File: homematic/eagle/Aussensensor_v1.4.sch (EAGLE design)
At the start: 41 parts, among them IC1 Atmega 328P, IC2 MAX1724, IC3 TSL2561, IC4 BMP180, IC5 BME280, IC6 DS18B20, T1 IRML6344

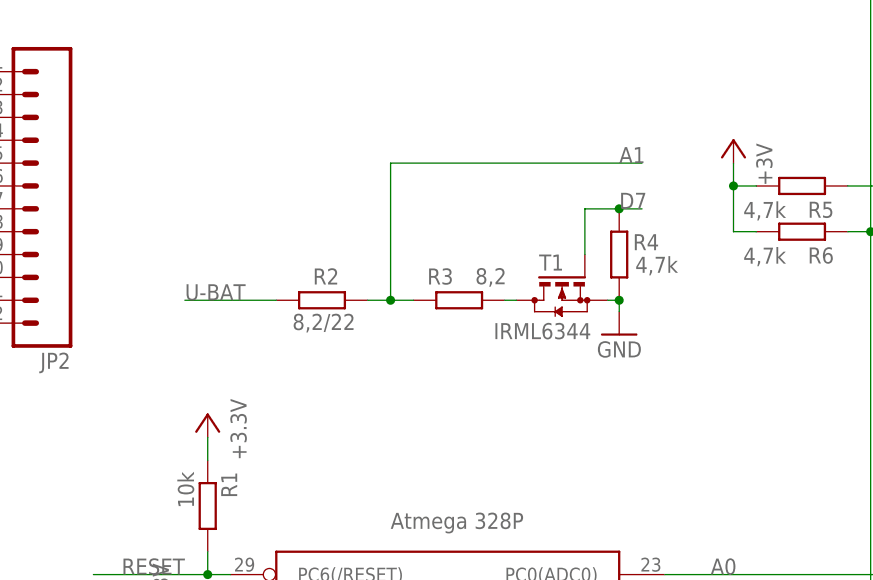
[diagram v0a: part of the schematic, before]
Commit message: added SJ2 for battery voltage measurement w/o battery load
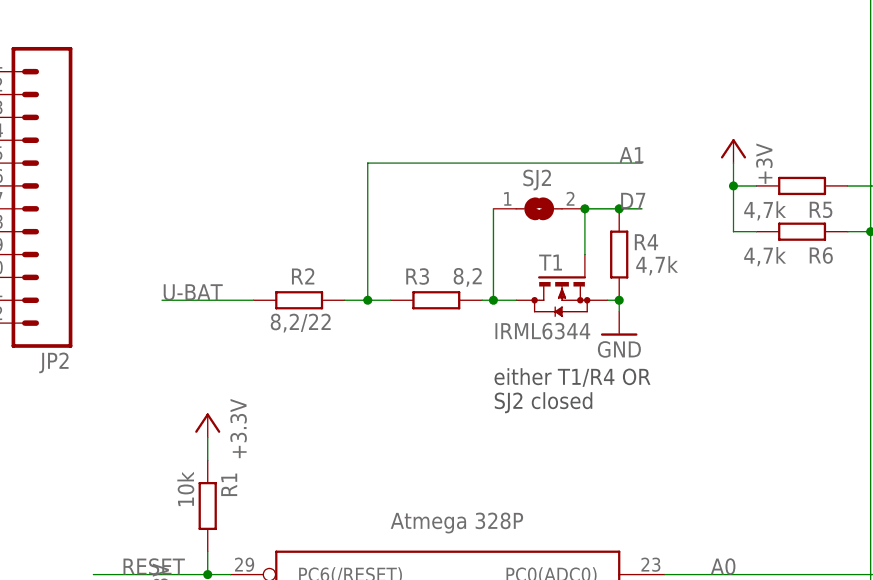
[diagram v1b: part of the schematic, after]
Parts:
- added SJ2: (no value), jumper:SJ
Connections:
- net D7: now also SJ2.2
- net N$3: now also SJ2.1
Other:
- note added: "either T1/R4 OR SJ2 closed"
- moved on the sheet: R2, R3
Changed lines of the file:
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@@
 <setting verticaltext="up"/>
 </settings>
-<grid distance="0.1" unitdist="inch" unit="inch" style="lines" multiple="1" display="no" altdistance="0.01" altunitdist="inch" altunit="inch"/>
+<grid distance="25" unitdist="mil" unit="mil" style="lines" multiple="1" display="no" altdistance="0.01" altunitdist="inch" altunit="inch"/>
 <layers>
 <layer number="1" name="Top" color="4" fill="1" visible="no" active="no"/>
@@
 <part name="R4" library="rcl" deviceset="R-EU_" device="M0805" value="4,7k"/>
 <part name="GND20" library="supply1" deviceset="GND" device=""/>
+<part name="SJ2" library="jumper" deviceset="SJ" device=""/>
 </parts>
 <sheets>
@@
 <text x="208.28" y="127" size="1.778" layer="97">I2C address: 0x77</text>
 <text x="208.28" y="106.68" size="1.778" layer="97" rot="MR180">I2C address: 0x76</text>
+<text x="120.65" y="124.46" size="1.778" layer="97" rot="MR180">either T1/R4 OR
+SJ2 closed</text>
 </plain>
 <instances>
-<instance part="IC1" gate="G$1" x="114.3" y="76.2"/>
+<instance part="IC1" gate="G$1" x="114.3" y="76.2" smashed="yes">
+<attribute name="NAME" x="96.52" y="35.56" size="1.778" layer="95"/>
+<attribute name="VALUE" x="109.22" y="106.68" size="1.778" layer="96"/>
+</instance>
 <instance part="R1" gate="G$1" x="88.9" y="109.22" rot="R270"/>
 <instance part="P+1" gate="1" x="88.9" y="119.38" rot="MR0"/>
@@
 <attribute name="NAME" x="158.115" y="62.23" size="1.778" layer="95"/>
 </instance>
-<instance part="R2" gate="G$1" x="101.6" y="132.08" smashed="yes">
-<attribute name="NAME" x="100.584" y="133.8326" size="1.778" layer="95"/>
-<attribute name="VALUE" x="98.298" y="128.778" size="1.778" layer="96"/>
-</instance>
-<instance part="R3" gate="G$1" x="116.84" y="132.08" smashed="yes">
-<attribute name="NAME" x="113.284" y="133.8326" size="1.778" layer="95"/>
-<attribute name="VALUE" x="118.618" y="133.858" size="1.778" layer="96"/>
+<instance part="R2" gate="G$1" x="99.06" y="132.08" smashed="yes">
+<attribute name="NAME" x="98.044" y="133.8326" size="1.778" layer="95"/>
+<attribute name="VALUE" x="95.758" y="128.778" size="1.778" layer="96"/>
+</instance>
+<instance part="R3" gate="G$1" x="114.3" y="132.08" smashed="yes">
+<attribute name="NAME" x="110.744" y="133.8326" size="1.778" layer="95"/>
+<attribute name="VALUE" x="116.078" y="133.858" size="1.778" layer="96"/>
 </instance>
 <instance part="FRAME1" gate="G$1" x="0" y="0"/>
@@
 </instance>
 <instance part="GND20" gate="1" x="134.62" y="128.27" rot="MR0"/>
+<instance part="SJ2" gate="1" x="125.73" y="142.24" smashed="yes">
+<attribute name="NAME" x="123.825" y="144.78" size="1.778" layer="95"/>
+<attribute name="VALUE" x="123.19" y="138.43" size="1.778" layer="96"/>
+</instance>
 </instances>
 <busses>
@@
 <wire x1="134.62" y1="142.24" x2="137.16" y2="142.24" width="0.1524" layer="91"/>
 <junction x="134.62" y="142.24"/>
+<pinref part="SJ2" gate="1" pin="2"/>
+<junction x="130.81" y="142.24"/>
 </segment>
 </net>
@@
 <pinref part="R3" gate="G$1" pin="1"/>
 <pinref part="R2" gate="G$1" pin="2"/>
+<wire x1="104.14" y1="132.08" x2="106.68" y2="132.08" width="0.1524" layer="91"/>
 <wire x1="106.68" y1="132.08" x2="109.22" y2="132.08" width="0.1524" layer="91"/>
-<wire x1="109.22" y1="132.08" x2="111.76" y2="132.08" width="0.1524" layer="91"/>
-<wire x1="109.22" y1="132.08" x2="109.22" y2="147.32" width="0.1524" layer="91"/>
-<junction x="109.22" y="132.08"/>
-<wire x1="109.22" y1="147.32" x2="137.16" y2="147.32" width="0.1524" layer="91"/>
+<wire x1="106.68" y1="132.08" x2="106.68" y2="147.32" width="0.1524" layer="91"/>
+<junction x="106.68" y="132.08"/>
+<wire x1="106.68" y1="147.32" x2="137.16" y2="147.32" width="0.1524" layer="91"/>
 <label x="134.62" y="147.32" size="1.778" layer="95"/>
 </segment>
@@
 <segment>
 <pinref part="R2" gate="G$1" pin="1"/>
-<wire x1="96.52" y1="132.08" x2="86.36" y2="132.08" width="0.1524" layer="91"/>
-<label x="86.36" y="132.08" size="1.778" layer="95"/>
+<wire x1="93.98" y1="132.08" x2="83.82" y2="132.08" width="0.1524" layer="91"/>
+<label x="83.82" y="132.08" size="1.778" layer="95"/>
 </segment>
 <segment>
@@
 <pinref part="T1" gate="G$1" pin="D"/>
 <pinref part="R3" gate="G$1" pin="2"/>
-<wire x1="123.19" y1="132.08" x2="121.92" y2="132.08" width="0.1524" layer="91"/>
+<wire x1="123.19" y1="132.08" x2="120.65" y2="132.08" width="0.1524" layer="91"/>
+<pinref part="SJ2" gate="1" pin="1"/>
+<wire x1="120.65" y1="132.08" x2="119.38" y2="132.08" width="0.1524" layer="91"/>
+<wire x1="120.65" y1="142.24" x2="120.65" y2="132.08" width="0.1524" layer="91"/>
+<junction x="120.65" y="132.08"/>
 </segment>
 </net>
@@
 </schematic>
 </drawing>
+<compatibility>
+<note version="6.3" minversion="6.2.2" severity="warning">
+Since Version 6.2.2 text objects can contain more than one line,
+which will not be processed correctly with this version.
+</note>
+</compatibility>
 </eagle>

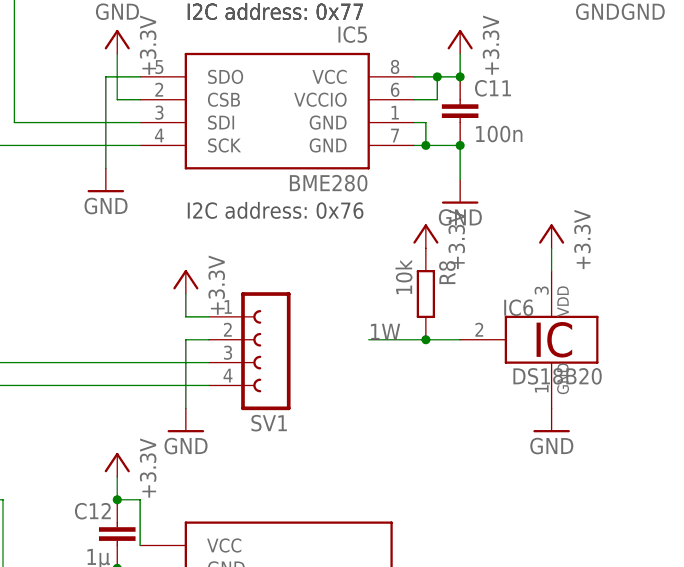
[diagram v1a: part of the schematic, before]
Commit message: replaced 10k by 4k7 for DS18x20 in Aussensensor v1.4 and v1.5
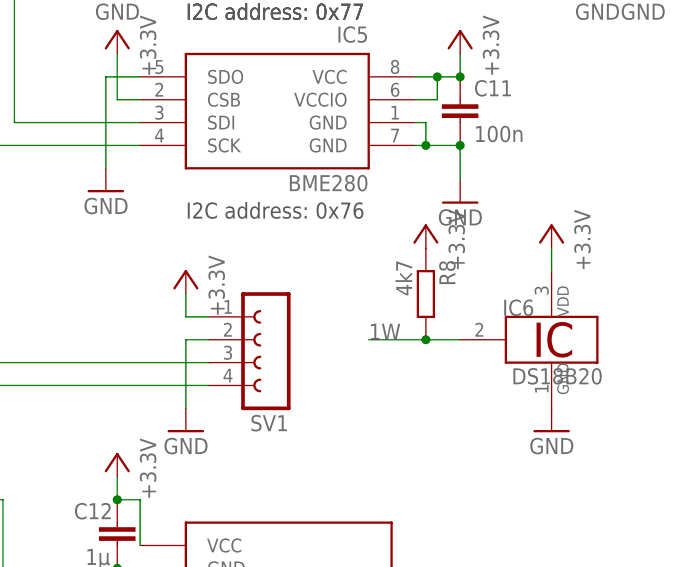
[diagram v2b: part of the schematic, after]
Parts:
- R8: value 10k -> 4k7
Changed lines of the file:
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@@
 <setting verticaltext="up"/>
 </settings>
-<grid distance="25" unitdist="mil" unit="mil" style="lines" multiple="1" display="no" altdistance="0.01" altunitdist="inch" altunit="inch"/>
+<grid distance="0.1" unitdist="inch" unit="inch" style="lines" multiple="1" display="no" altdistance="0.01" altunitdist="inch" altunit="inch"/>
 <layers>
 <layer number="1" name="Top" color="4" fill="1" visible="no" active="no"/>
@@
 <part name="P+11" library="supply1" deviceset="+5V" device="" value="+3.3V"/>
 <part name="GND21" library="supply1" deviceset="GND" device=""/>
-<part name="R8" library="rcl" deviceset="R-EU_" device="M0805" value="10k"/>
+<part name="R8" library="rcl" deviceset="R-EU_" device="M0805" value="4k7"/>
 <part name="P+12" library="supply1" deviceset="+5V" device="" value="+3.3V"/>
 <part name="C12" library="rcl" deviceset="C-EU" device="C0805" value="1µ"/>
